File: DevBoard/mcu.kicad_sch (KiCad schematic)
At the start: 44 parts, among them J301 SWD, J302 UART debug, J303 Spare GPIO, SW301 RESET, U301 CC2340R5MODA, U302 TMP1075, U303 TMP1075, U304 TMP1075, U305 TMP1075, U306 TMP1075

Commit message: Dev board BOM: rev A7 costing, LCSC numbers for the new parts
TMP1075DSGR C2870250, 15 pF C76950, 1 pF C76952, 0R C17168, 470k C23178.
U301 (CC2340R5MODA) left unpriced: 0 stock at JLC, out of stock at TI.
5 boards: $51.13 parts + $20.40 fees = $71.53/board excluding U301.

Co-Authored-By: Claude Opus 5.5 <noreply@anthropic.com>
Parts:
- C313: LCSC (none) -> C76950
- C315: LCSC (none) -> C76952
- R313: LCSC (none) -> C23178; MPN (none) -> 0603WAF4703T5E
- R321: LCSC (none) -> C17168
- U302, U303, U304, U305, U306: LCSC (none) -> C2870250
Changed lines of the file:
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@@
 			)
 		)
-		(property "LCSC" ""
+		(property "LCSC" "C23178"
 			(at 81.28 44.45 0)
 			(hide yes)
@@
 			)
 		)
-		(property "MPN" ""
+		(property "MPN" "0603WAF4703T5E"
 			(at 81.28 44.45 0)
 			(hide yes)
@@
 			)
 		)
-		(property "LCSC" ""
+		(property "LCSC" "C76950"
 			(at 180.34 106.68 0)
 			(hide yes)
@@
 			)
 		)
-		(property "LCSC" ""
+		(property "LCSC" "C17168"
 			(at 187.96 106.68 0)
 			(hide yes)
@@
 			)
 		)
-		(property "LCSC" ""
+		(property "LCSC" "C76952"
 			(at 191.77 110.49 0)
 			(hide yes)
@@
 			)
 		)
-		(property "LCSC" ""
+		(property "LCSC" "C2870250"
 			(at 60.96 200.66 0)
 			(hide yes)
@@
 			)
 		)
-		(property "LCSC" ""
+		(property "LCSC" "C2870250"
 			(at 101.6 200.66 0)
 			(hide yes)
@@
 			)
 		)
-		(property "LCSC" ""
+		(property "LCSC" "C2870250"
 			(at 142.24 200.66 0)
 			(hide yes)
@@
 			)
 		)
-		(property "LCSC" ""
+		(property "LCSC" "C2870250"
 			(at 124.46 241.3 0)
 			(hide yes)
@@
 			)
 		)
-		(property "LCSC" ""
+		(property "LCSC" "C2870250"
 			(at 165.1 241.3 0)
 			(hide yes)

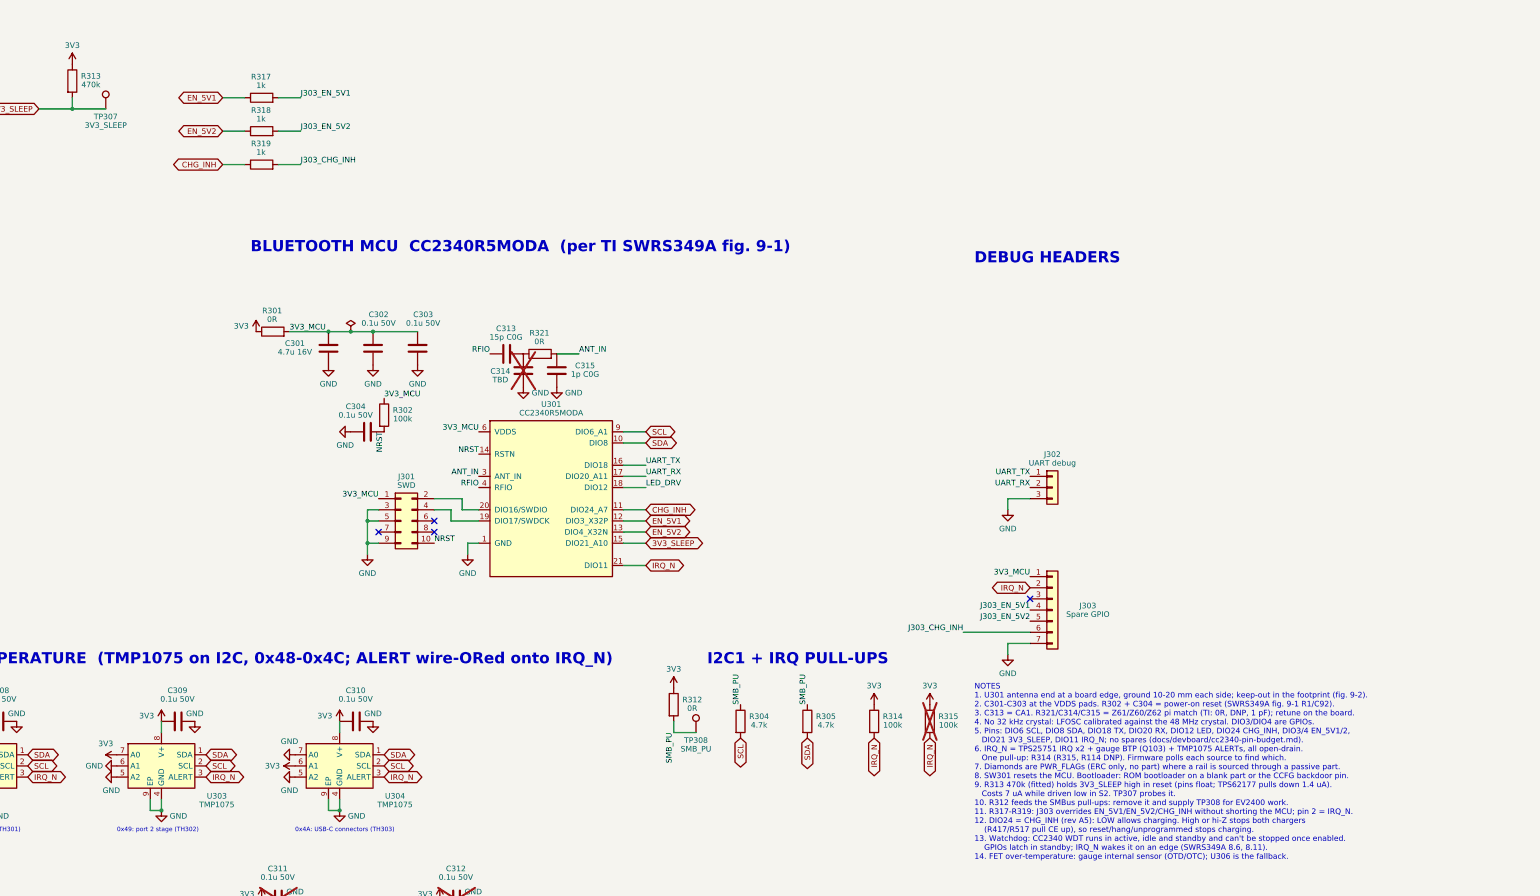
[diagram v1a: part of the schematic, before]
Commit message: Dev board rev A8: review 4 pre-routing hardware fixes
Applied by tools/review4_fixes.py (one-shot from the rev A7 sheets);
part numbers checked against JLC's parts API.
- R313 470k -> 220k (3V3_SLEEP margin), R314 100k -> 47k (IRQ_N),
  R304/R305 4.7k -> 3.3k (I2C rise time)
- R322/R323 1k in series with J302 TX/RX; R324 1k at J303 pin 2
- C314 placeholder 1p C0G (DNP); C401/C402 330p -> 220p (CC capacitance)
- R450/R451 snubber resistors -> 1206 0.66 W (a 2010/0612 doesn't fit)
- D401/D501 SMAJ22A -> TVS2200DRVR flat clamp (stock KiCad symbol and
  footprint; datasheet added)
- TP415-TP421 (+5xx) 1 mm probe pads on CC, SBU and liquid-detect nets
Board synced and placed (place_blocks.py): 428 parts, 0 parity issues,
no courtyard overlaps. ERC: the 8 known warnings. README item 41,
schematic PDF and placement PNG regenerated.

Co-Authored-By: Claude Opus 5.5 <noreply@anthropic.com>
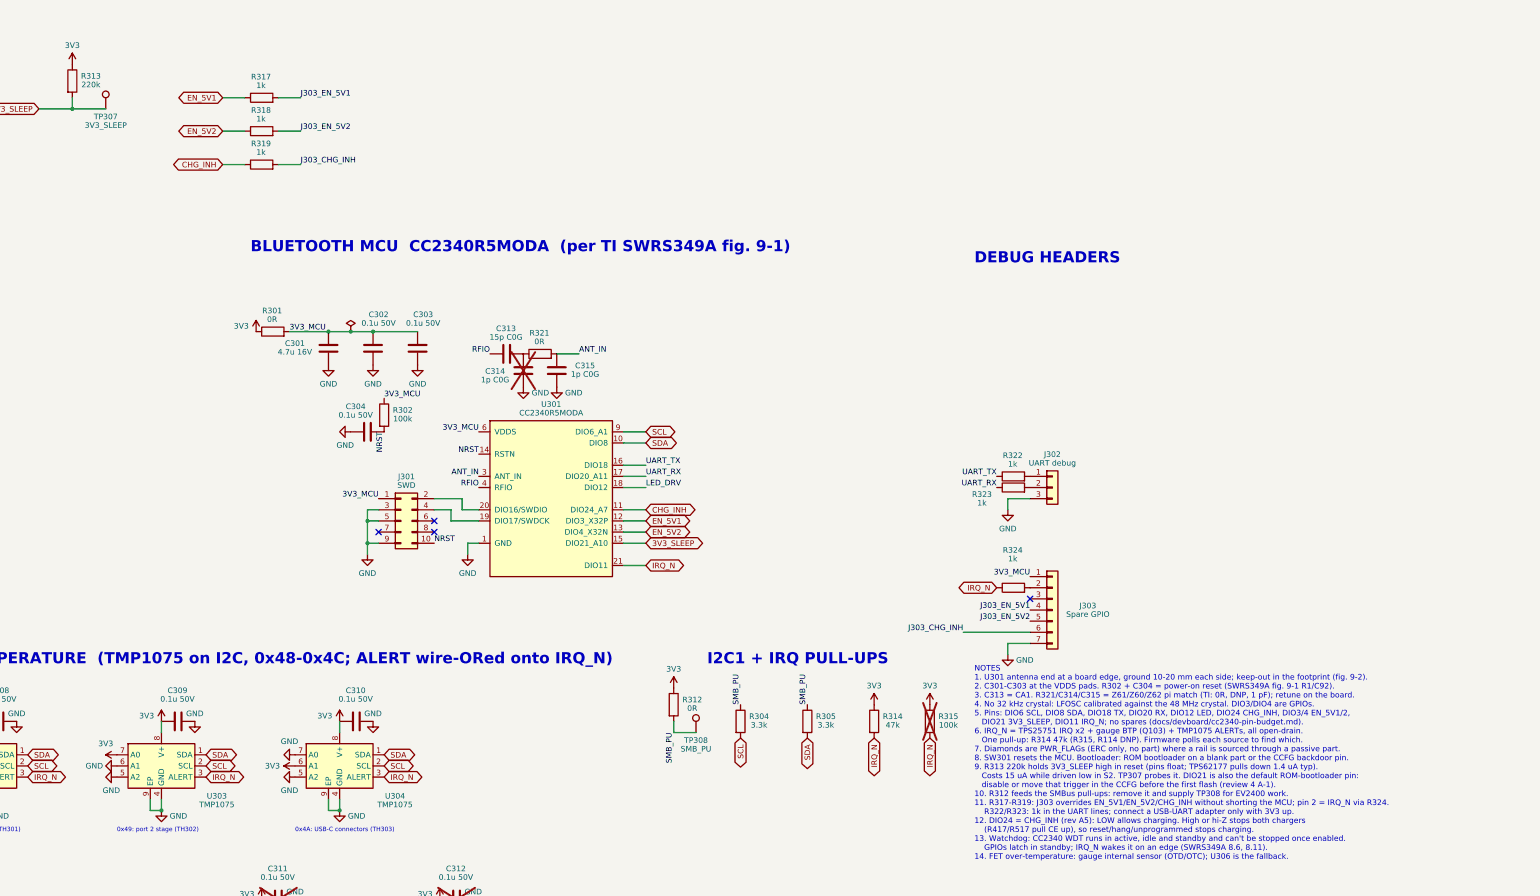
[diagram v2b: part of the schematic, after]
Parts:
- added R322, R323, R324: 1k, Resistor_SMD:R_0603_1608Metric, symbol Device:R
- C314: value TBD -> 1p C0G; LCSC (none) -> C76952; MPN (none) -> GRM1555C1H1R0BA01D; Notes (none) -> Z60 shunt, DNP as on TI's LaunchPad. Placeholder value: TI 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
- R304, R305: value 4.7k -> 3.3k; LCSC C23162 -> C22978; MPN 0603WAF4701T5E -> 0603WAF3301T5E
- R313: value 470k -> 220k; LCSC C23178 -> C22961; MPN 0603WAF4703T5E -> 0603WAF2203T5E; Notes DNP: fit to keep the TPS62177 out of sleep mode (15 mA max)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 -> 3V3_SLEEP pull-up: holds the TPS62177 in normal mode while 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
- R314: value 100k -> 47k; LCSC C25803 -> C25819; MPN 0603WAF1003T5E -> 0603WAF4702T5E; Notes TPS25751 I2Ct_IRQ is open drain and needs an external pull-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 -> The one IRQ_N pull-up (TPS25751 I2Ct_IRQ x2, gauge BTP via 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
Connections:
- net IRQ_N: now also R324.1; no longer J303.2 (Pin_2)
- net UART_RX: now also R323.1; no longer J302.2 (Pin_2)
- net UART_TX: now also R322.1; no longer J302.1 (Pin_1)
- new net: J302.2 (Pin_2), R323.2
- new net: J302.1 (Pin_1), R322.2
- new net: J303.2 (Pin_2), R324.2

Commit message: Dev board rev A8 part 2: review 4 docs, BOM, A-2 procedure, J104 clamp
Schematic edits by tools/review4_docs.py (helpers split out of
review4_fixes.py into tools/sch_edit.py; review4_fixes output unchanged).
- A-2: EV2400 work only with 3V3 up (J104) and U301 in reset; checklist,
  R312/R301 Notes and MCU sheet note 10 rewritten.
- D-5: D105 SMAJ18A clamp on the J104 side of D104; board placed
  (D104 moved one body width left).
- Stale Notes, sheet notes, heading and address text fixed; sheet 4
  renamed "MCU and Sensors"; revision log A7/A8; title blocks A8.
- MPNs filled on the parts that had only LCSC numbers; Sourcing on U301
  and J301; J301 out of the position file.
- bringup-config-checklist, mcu-io-power-states and power-budget rewritten
  for the CC2340 with every review 4 CONFIG item; corrections in
  circuit-description, cost-down and cc2340-pin-budget.
ERC: 8 known warnings. 0 text overlaps. DRC: 0 parity issues, no
courtyard overlaps (429 parts). README item 42.

Co-Authored-By: Claude Opus 5.5 <noreply@anthropic.com>
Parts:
- J301: Sourcing (none) -> Hand-fit, not JLC assembled. Samtec part to be replaced by 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
- R301: Notes MCU 3V3 link -> 3V3 -> 3V3_MCU link (VDDS). Never remove it while 3V3 is up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
- R302: Notes TPS25751 I2Ct_IRQ is open drain and needs an external pull-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 -> RSTN pull-up: SWRS349A fig. 9-1 R1 (100k), with C304 = C92 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
- R312: Notes Remove to isolate the SMBus pull-ups from 3V3 (dead 3V3 = 4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 -> Feeds the SMBus/I2C pull-ups from 3V3. Keep it fitted: do E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
- R315: Notes TPS25751 I2Ct_IRQ is open drain and needs an external pull-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 -> DNP spare IRQ_N pull-up (R314 is the one fitted)
- R319: Notes Series resistor to J303: CHG_INH can be forced from the header without fighting PB8 -> Series resistor to J303: CHG_INH can be forced from the header without fighting DIO24
- R321: Notes MCU 3V3 link -> Z61 series element of the antenna pi match (TI LaunchPad: 0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
- U301: Sourcing (none) -> TI.com (CC2340R5MODAN0MHAR), consigned to JLC for placement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
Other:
- note added: "I2C0 + IRQ PULL-UPS"
- note removed: "I2C1 + IRQ PULL-UPS"
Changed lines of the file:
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@@
 		(title "MCU and board temperature")
 		(date "2026-10-14")
-		(rev "A7")
+		(rev "A8")
 		(company "Monolith 100 W battery bank - dev board")
 		(comment 1 "CC2340R5MODA, debug headers, TMP1075 x3 (+2 DNP)")
@@
 		(comment 3 "Reviewed 3x (docs/devboard); board placed, not routed or built")
 	)
-	(text "NOTES\n1. U301 antenna end at a board edge, ground 10-20 mm each side; keep-out in the footprint (fig. 9-2).\n2. C301-C303 at the VDDS pads. R302 + C304 = power-on reset (SWRS349A fig. 9-1 R1/C92).\n3. C313 = CA1. R321/C314/C315 = Z61/Z60/Z62 pi match (TI: 0R, DNP, 1 pF); retune on the board.\n4. No 32 kHz crystal: LFOSC calibrated against the 48 MHz crystal. DIO3/DIO4 are GPIOs.\n5. Pins: DIO6 SCL, DIO8 SDA, DIO18 TX, DIO20 RX, DIO12 LED, DIO24 CHG_INH, DIO3/4 EN_5V1/2,\n   DIO21 3V3_SLEEP, DIO11 IRQ_N; no spares (docs/devboard/cc2340-pin-budget.md).\n6. IRQ_N = TPS25751 IRQ x2 + gauge BTP (Q103) + TMP1075 ALERTs, all open-drain.\n   One pull-up: R314 47k (R315, R114 DNP). Firmware polls each source to find which.\n7. Diamonds are PWR_FLAGs (ERC only, no part) where a rail is sourced through a passive part.\n8. SW301 resets the MCU. Bootloader: ROM bootloader on a blank part or the CCFG backdoor pin.\n9. R313 220k holds 3V3_SLEEP high in reset (pins float; TPS62177 pulls down 1.4 uA typ).\n   Costs 15 uA while driven low in S2. TP307 probes it. DIO21 is also the default ROM-bootloader pin:\n   disable or move that trigger in the CCFG before the first flash (review 4 A-1).\n10. R312 feeds the SMBus pull-ups: remove it and supply TP308 for EV2400 work.\n11. R317-R319: J303 overrides EN_5V1/EN_5V2/CHG_INH without shorting the MCU; pin 2 = IRQ_N via R324.\n    R322/R323: 1k in the UART lines; connect a USB-UART adapter only with 3V3 up.\n12. DIO24 = CHG_INH (rev A5): LOW allows charging. High or hi-Z stops both chargers\n    (R417/R517 pull CE up), so reset/hang/unprogrammed stops charging.\n13. Watchdog: CC2340 WDT runs in active, idle and standby and can't be stopped once enabled.\n    GPIOs latch in standby; IRQ_N wakes it on an edge (SWRS349A 8.6, 8.11).\n14. FET over-temperature: gauge internal sensor (OTD/OTC); U306 is the fallback."
+	(text "NOTES\n1. U301 antenna end at a board edge, ground 10-20 mm each side; keep-out in the footprint (fig. 9-2).\n2. C301-C303 at the VDDS pads. R302 + C304 = power-on reset (SWRS349A fig. 9-1 R1/C92).\n3. C313 = CA1. R321/C314/C315 = Z61/Z60/Z62 pi match (TI: 0R, DNP, 1 pF); retune on the board.\n4. No 32 kHz crystal: LFOSC calibrated against the 48 MHz crystal. DIO3/DIO4 are GPIOs.\n5. Pins: DIO6 SCL, DIO8 SDA, DIO18 TX, DIO20 RX, DIO12 LED, DIO24 CHG_INH, DIO3/4 EN_5V1/2,\n   DIO21 3V3_SLEEP, DIO11 IRQ_N; no spares (docs/devboard/cc2340-pin-budget.md).\n6. IRQ_N = TPS25751 IRQ x2 + gauge BTP (Q103) + TMP1075 ALERTs, all open-drain.\n   One pull-up: R314 47k (R315, R114 DNP). Firmware polls each source to find which.\n7. Diamonds are PWR_FLAGs (ERC only, no part) where a rail is sourced through a passive part.\n8. SW301 resets the MCU. Bootloader: ROM bootloader on a blank part or the CCFG backdoor pin.\n9. R313 220k holds 3V3_SLEEP high in reset (pins float; TPS62177 pulls down 1.4 uA typ).\n   Costs 15 uA while driven low in S2. TP307 probes it. DIO21 is also the default ROM-bootloader pin:\n   disable or move that trigger in the CCFG before the first flash (review 4 A-1).\n10. R312 feeds the SMBus pull-ups. EV2400 work only with 3V3 up (J104 powered) and U301 held in reset:\n    an unpowered CC2340 can't take bus voltage (VDDS + 0.3 V max). Never feed TP308 with 3V3 down (review 4 A-2).\n11. R317-R319: J303 overrides EN_5V1/EN_5V2/CHG_INH without shorting the MCU; pin 2 = IRQ_N via R324.\n    R322/R323: 1k in the UART lines; connect a USB-UART adapter only with 3V3 up.\n12. DIO24 = CHG_INH (rev A5): LOW allows charging. High or hi-Z stops both chargers\n    (R417/R517 pull CE up), so reset/hang/unprogrammed stops charging.\n13. Watchdog: CC2340 WDT runs in active, idle and standby and can't be stopped once enabled.\n    GPIOs latch in standby; IRQ_N wakes it on an edge (SWRS349A 8.6, 8.11).\n14. FET over-temperature: gauge internal sensor (OTD/OTC); U306 is the fallback."
 		(exclude_from_sim no)
-		(at 287.02 222.25 0)
+		(at 287.02 224.79 0)
 		(effects
 			(font
@@
 		)
 	)
-	(text "I2C1 + IRQ PULL-UPS"
+	(text "I2C0 + IRQ PULL-UPS"
 		(exclude_from_sim no)
 		(at 226.06 177.8 0)
@@
 			)
 		)
-		(property "Notes" "MCU 3V3 link"
+		(property "Notes" "3V3 -> 3V3_MCU link (VDDS). Never remove it while 3V3 is up: the bus pull-ups would then drive SCL/SDA of an unpowered U301 above its VDDS + 0.3 V abs max (review 4 A-2)"
 			(at 0 0 0)
 			(hide yes)
@@
 		(in_bom yes)
 		(on_board yes)
-		(in_pos_files yes)
+		(in_pos_files no)
 		(dnp no)
 		(property "Reference" "J301"
@@
 			)
 		)
+		(property "Sourcing" "Hand-fit, not JLC assembled. Samtec part to be replaced by an unkeyed 2x5 1.27 mm header JLC stocks (silk shows pin 1 and the cable-key side)"
+			(at 156.21 144.78 0)
+			(hide yes)
+			(show_name no)
+			(do_not_autoplace no)
+			(effects
+				(font
+					(size 1.27 1.27)
+				)
+			)
+		)
 		(pin "1"
 		)
@@
 			)
 		)
-		(property "Notes" "TPS25751 I2Ct_IRQ is open drain and needs an external pull-up (Table 5-1)"
+		(property "Notes" "DNP spare IRQ_N pull-up (R314 is the one fitted)"
 			(at 276.86 190.5 0)
 			(hide yes)
@@
 			)
 		)
-		(property "Notes" "Remove to isolate the SMBus pull-ups from 3V3 (dead 3V3 = 4.7k pull-downs); then feed TP308 for EV2400 work"
+		(property "Notes" "Feeds the SMBus/I2C pull-ups from 3V3. Keep it fitted: do EV2400 work with J104 powered (3V3 up) and U301 held in reset (SW301 or J301 nRESET). Feeding TP308 with 3V3 down drives the unpowered CC2340's SCL/SDA above its VDDS + 0.3 V abs max (review 4 A-2)"
 			(at 218.44 186.69 0)
 			(hide yes)
@@
 			)
 		)
-		(property "Notes" "Series resistor to J303: CHG_INH can be forced from the header without fighting PB8"
+		(property "Notes" "Series resistor to J303: CHG_INH can be forced from the header without fighting DIO24"
 			(at 124.46 63.5 0)
 			(hide yes)
@@
 			)
 		)
+		(property "Sourcing" "TI.com (CC2340R5MODAN0MHAR), consigned to JLC for placement; JLC C55046847 had no stock on 2026-10-14"
+			(at 190.5 139.7 0)
+			(hide yes)
+			(show_name no)
+			(do_not_autoplace no)
+			(effects
+				(font
+					(size 1.27 1.27)
+				)
+			)
+		)
 		(pin "1"
 		)
@@
 			)
 		)
-		(property "Notes" "TPS25751 I2Ct_IRQ is open drain and needs an external pull-up (Table 5-1)"
+		(property "Notes" "RSTN pull-up: SWRS349A fig. 9-1 R1 (100k), with C304 = C92 as the power-on reset"
 			(at 152.4 120.65 0)
 			(hide yes)
@@
 			)
 		)
-		(property "Notes" "MCU 3V3 link"
+		(property "Notes" "Z61 series element of the antenna pi match (TI LaunchPad: 0R). Retune on this board"
 			(at 60.96 5.08 0)
 			(hide yes)

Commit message: Dev board: hybrid battery-side bulk, ship mode at 5 % SOC, CC2340 in stock
- C432/C532 (battery-side bulk, the only bulk cap biased in idle) ->
  Panasonic EEH-ZA1E101XP hybrid polymer (C264047), CP_Elec_6.3x7.7.
  Same 100 uF / 30 mOhm as the JIERR solid polymer, but leakage limit
  0.01CV = 25 uA instead of 0.2CV = 500 uA. +$1.28 per board. README
  item 43; review 4 B-4 closed. Board synced: 0 parity issues, no
  courtyard overlaps.
- Ship mode also triggers at RSOC <= 5 % (checklist, power states,
  review 4 S-1).
- CC2340R5MODA is in stock at TI.com (seen logged in, 2026-10-15):
  U301 Sourcing, bom_cost.py, checklist and README notes updated.

Co-Authored-By: Claude Opus 5.5 <noreply@anthropic.com>
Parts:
- U301: Sourcing TI.com (CC2340R5MODAN0MHAR), consigned to JLC for placement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 -> TI.com (CC2340R5MODAN0MHAR, in stock 2026-10-15), consigned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
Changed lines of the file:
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@@
 			)
 		)
-		(property "Sourcing" "TI.com (CC2340R5MODAN0MHAR), consigned to JLC for placement; JLC C55046847 had no stock on 2026-10-14"
+		(property "Sourcing" "TI.com (CC2340R5MODAN0MHAR, in stock 2026-10-15), consigned to JLC for placement; JLC C55046847 had no stock on 2026-10-14"
 			(at 190.5 139.7 0)
 			(hide yes)

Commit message: Dev board: cut JLC extended parts 37 -> 27 for a 2-board build
tools/bom_fee_cut.py (one-shot); README item 44. At 2 boards the costed
BOM goes from $124.28 to $108.49 per board.
- Basic/preferred swaps, no footprint changes: C313 -> C1548, C315/C314
  -> C1550, C401/C402 -> C1530 (X7R), R433/R434 -> 120k/22k 1 %
  (PP5V 5.16 V), C443/C543 -> 100 uF 35 V Honor polymer (same as C421).
- Hand-fit from LCSC: BT101-BT104, the 13 Harwin test loops, U202, D105
  (dev-only; out of the position file).
- Board: fields refreshed by netlist_to_board.py; also includes Logan's
  block move made in KiCad. DRC parity 0; ERC unchanged.

Co-Authored-By: Claude Opus 5.5 <noreply@anthropic.com>
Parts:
- C313: LCSC C76950 -> C1548; MPN GRM1555C1H150JA01D -> 0402CG150J500NT
- C314, C315: LCSC C76952 -> C1550; MPN GRM1555C1H1R0BA01D -> 0402CG1R0C500NT
- TP309: LCSC C55121754 -> (none); Sourcing (none) -> Hand-solder, not JLC assembled (test loop, dev only; saves 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
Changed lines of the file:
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@@
 		(in_bom yes)
 		(on_board yes)
-		(in_pos_files yes)
+		(in_pos_files no)
 		(dnp no)
 		(property "Reference" "TP309"
@@
 			)
 		)
-		(property "LCSC" "C55121754"
+		(property "LCSC" ""
 			(at 307.34 241.3 0)
 			(hide yes)
@@
 			)
 		)
+		(property "Sourcing" "Hand-solder, not JLC assembled (test loop, dev only; saves a JLC extended-part fee; LCSC C55121754 RH-S2761-46R (ronghe; Harwin S2761-46R equivalent))"
+			(at 307.34 241.3 0)
+			(hide yes)
+			(show_name no)
+			(do_not_autoplace no)
+			(effects
+				(font
+					(size 1.27 1.27)
+				)
+			)
+		)
 		(pin "1"
 		)
@@
 			)
 		)
-		(property "LCSC" "C76950"
+		(property "LCSC" "C1548"
 			(at 180.34 106.68 0)
 			(hide yes)
@@
 			)
 		)
-		(property "MPN" "GRM1555C1H150JA01D"
+		(property "MPN" "0402CG150J500NT"
 			(at 180.34 106.68 0)
 			(hide yes)
@@
 			)
 		)
-		(property "LCSC" "C76952"
+		(property "LCSC" "C1550"
 			(at 184.15 110.49 0)
 			(hide yes)
@@
 			)
 		)
-		(property "MPN" "GRM1555C1H1R0BA01D"
+		(property "MPN" "0402CG1R0C500NT"
 			(at 184.15 110.49 0)
 			(hide yes)
@@
 			)
 		)
-		(property "LCSC" "C76952"
+		(property "LCSC" "C1550"
 			(at 191.77 110.49 0)
 			(hide yes)
@@
 			)
 		)
-		(property "MPN" "GRM1555C1H1R0BA01D"
+		(property "MPN" "0402CG1R0C500NT"
 			(at 191.77 110.49 0)
 			(hide yes)
